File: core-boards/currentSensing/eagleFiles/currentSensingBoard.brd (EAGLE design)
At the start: 52 x 64.6 mm, 25 parts, among them J1 4-PIN_2MM-H, J2 3-PIN_2MM-H, J3 2-PIN_2MM-H, Q1 16MHz, X1 057-006-1

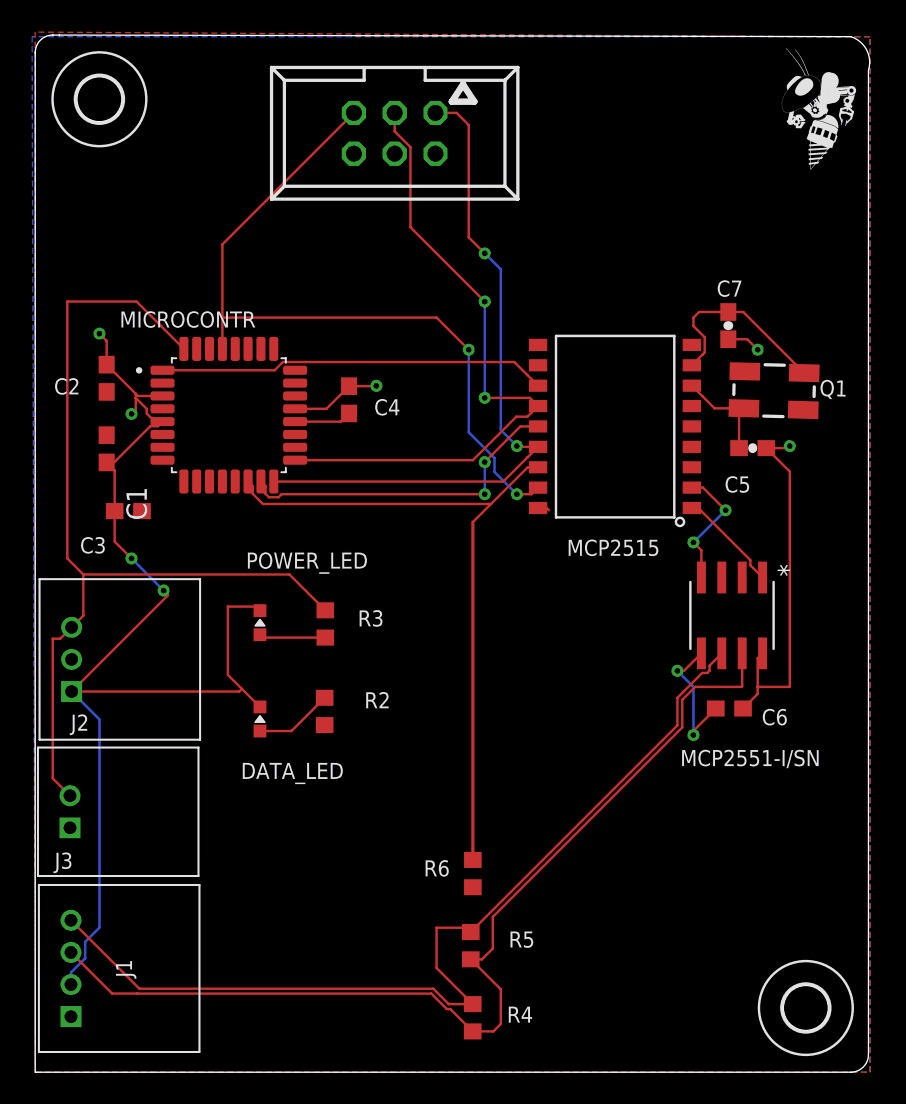
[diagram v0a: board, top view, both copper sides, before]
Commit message: Near-Finalized Current Sensing Board
I can't get the bottom edge to be round
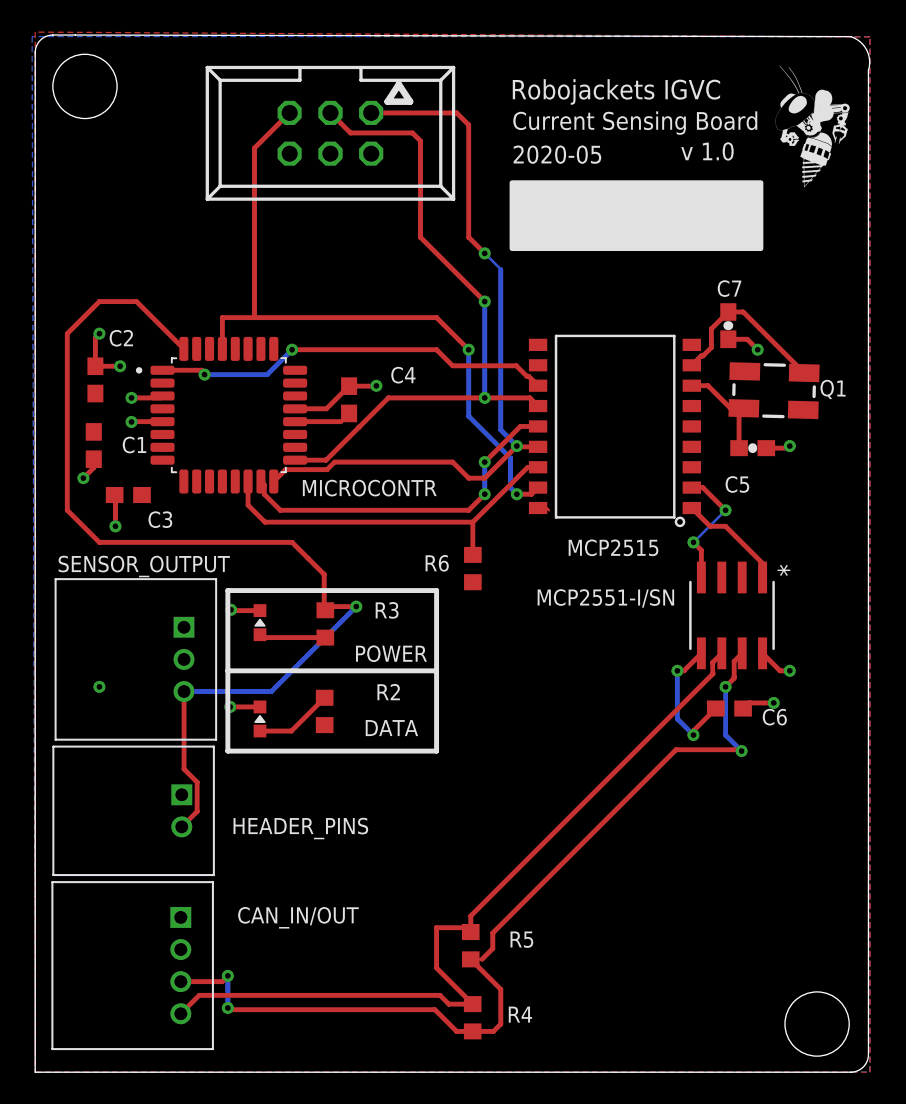
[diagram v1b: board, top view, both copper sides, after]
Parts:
- removed J1: 4-PIN_2MM-H, RoboJackets-Connectors:2MM-4-H
- removed J2: 3-PIN_2MM-H, RoboJackets-Connectors:2MM-3-H
- removed J3: 2-PIN_2MM-H, RoboJackets-Connectors:2MM-2-H
- removed U$2, U$3: (no value), holes:2,8
- removed X1: 057-006-1, con-panduit:057-006-1
- added CAN_IN/OUT: 4-PIN_2MM-H, RoboJackets-Connectors:2MM-4-H
- added HEADER_PINS: 2-PIN_2MM-H, RoboJackets-Connectors:2MM-2-H
- added ICSP: 057-006-1, con-panduit:057-006-1
- added SENSOR_OUTPUT: 3-PIN_2MM-H, RoboJackets-Connectors:2MM-3-H
- moved R6 19.0 mm to (27.3, 31.4)
- moved U$1 1.17 mm to (47.9, 55.1)
- moved C3 1.00 mm to (5.80, 36.0)
- moved C1 0.82 mm to (3.65, 39.0)
- moved C2 0.71 mm to (3.75, 43.1)
- renumbered DATA_LED to DATA, POWER_LED to POWER
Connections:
- net !RS: now also ICSP.5; no longer X1.5
- net +5V: now also CAN_IN/OUT.1, HEADER_PINS.1; no longer J1.1, J3.1
- net CAN_N: now also CAN_IN/OUT.4; no longer J1.4
- net CAN_P: now also CAN_IN/OUT.3; no longer J1.3
- net GND: now also CAN_IN/OUT.2, SENSOR_OUTPUT.1; no longer J1.2, J2.1
- net MISO: now also ICSP.1; no longer X1.1
- net SCK: now also ICSP.3; no longer X1.3
- net SENSOR_OUTPUT: now also HEADER_PINS.2, SENSOR_OUTPUT.3; no longer J2.3, J3.2
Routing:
- net GND: track 103.4 -> 28.6 mm, vias 7 -> 14
- net CAN_CS: track 42.5 -> 23.4 mm
- net CAN_N: track 59.1 -> 50.7 mm
- net SENSOR_OUTPUT: track 57.2 -> 64.1 mm, vias 0 -> 1
- net CAN_P: track 62.0 -> 57.5 mm, vias 0 -> 4
- net MISO: track 42.3 -> 45.8 mm
- net !RS: track 46.0 -> 43.5 mm
- net N$17: track 12.2 -> 10.8 mm
- net CAN_INT: track 24.2 -> 25.2 mm, vias 0 -> 2
- net SCK: track 40.1 -> 40.9 mm
- net MOSI: track 20.9 -> 21.7 mm
- net CAN_TX: track 6.23 -> 6.83 mm
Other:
- outline, holes or cut-outs redrawn
- board text added: "2020-05"
- board text added: "CAN_N"
- board text added: "CAN_P"
- board text added: "Current Sensing Board"
- board text added: "Robojackets IGVC"
- board text added: "v 1.0"

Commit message: Basic Updates Based on Notes
Needs help with a few things but I will discuss them in meeting.
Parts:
- moved DATA 6.94 mm to (20.1, 18.7)
- moved POWER 6.94 mm to (20.1, 24.7)
- moved R3 6.94 mm to (24.2, 24.6)
- moved R2 6.94 mm to (24.1, 19.2)
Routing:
- net SENSOR_OUTPUT: track 64.1 -> 75.9 mm, vias 1 -> 2

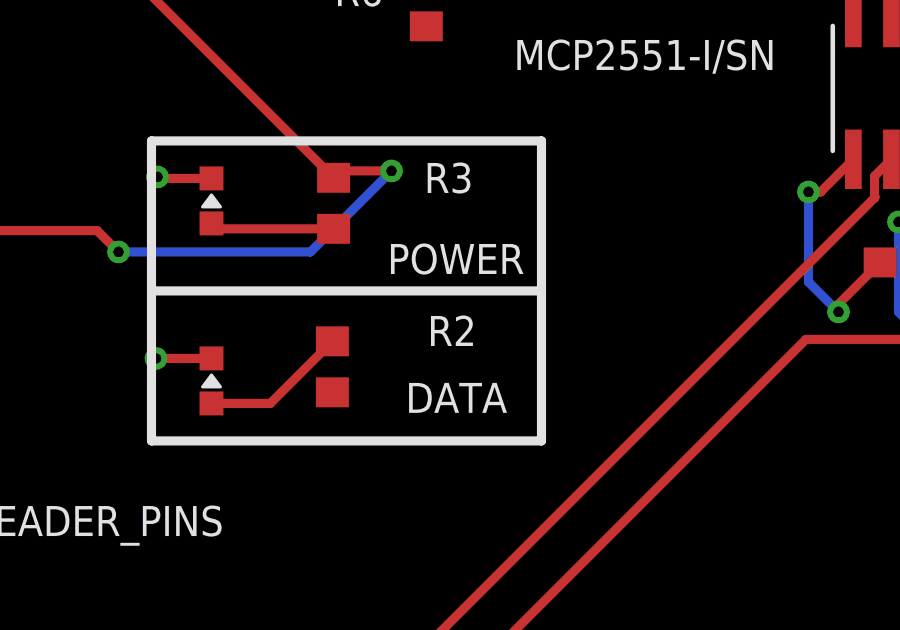
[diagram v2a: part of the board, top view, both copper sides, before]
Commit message: Leds fixed
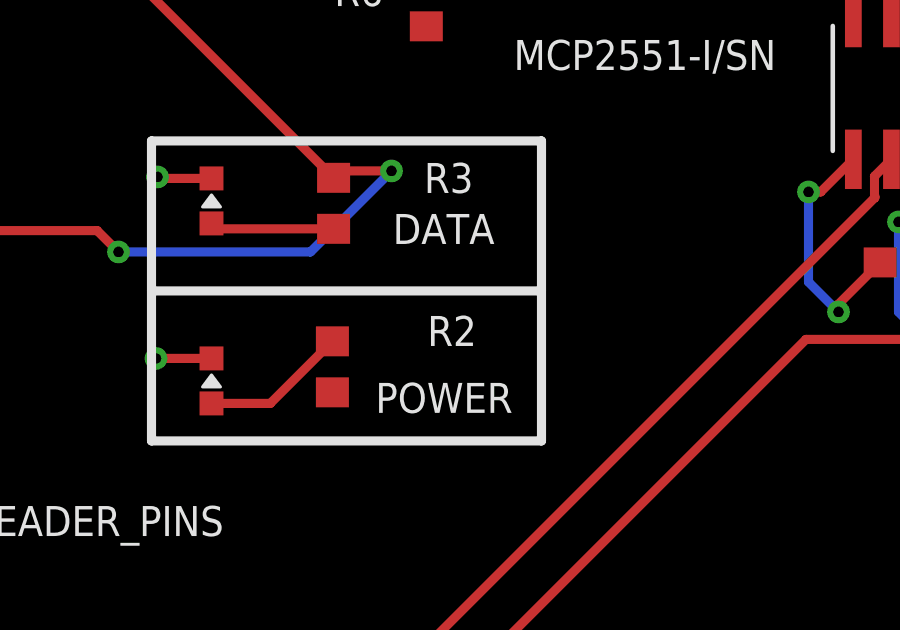
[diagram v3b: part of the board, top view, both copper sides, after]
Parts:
- DATA: value GREEN -> BLUE
- POWER: value BLUE -> GREEN
- moved DATA 6.00 mm to (20.1, 24.7)
- moved POWER 6.00 mm to (20.1, 18.7)
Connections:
- net N$2: now also DATA.A; no longer POWER.A
- net N$7: now also POWER.A; no longer DATA.A
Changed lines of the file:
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@@
 <attribute name="VALUE" x="24.2" y="53.93" size="1.778" layer="27" rot="R180"/>
 </element>
-<element name="DATA" library="RoboJackets-LEDs" package="CHIP-LED0603" value="GREEN" x="20.1" y="18.7" smashed="yes">
+<element name="POWER" library="RoboJackets-LEDs" package="CHIP-LED0603" value="GREEN" x="20.1" y="18.7" smashed="yes">
 <attribute name="DIGIKEY" value="160-1446-1-ND" x="20.1" y="18.7" size="1.778" layer="27" display="off"/>
 <attribute name="MPN" value="LTST-C191KGKT" x="20.1" y="18.7" size="1.778" layer="27" display="off"/>
-<attribute name="NAME" x="26.565" y="17.635" size="1" layer="25"/>
+<attribute name="NAME" x="25.565" y="17.635" size="1" layer="25"/>
 <attribute name="VALUE" x="22.005" y="18.065" size="1.27" layer="27" rot="R90"/>
 </element>
-<element name="POWER" library="RoboJackets-LEDs" package="CHIP-LED0603" value="BLUE" x="20.1" y="24.7" smashed="yes">
+<element name="DATA" library="RoboJackets-LEDs" package="CHIP-LED0603" value="BLUE" x="20.1" y="24.7" smashed="yes">
 <attribute name="DIGIKEY" value="160-1647-1-ND" x="20.1" y="24.7" size="1.778" layer="27" display="off"/>
 <attribute name="MPN" value="LTST-C191TBKT" x="20.1" y="24.7" size="1.778" layer="27" display="off"/>
-<attribute name="NAME" x="30.535" y="23.265" size="1" layer="25" rot="R180"/>
+<attribute name="NAME" x="29.535" y="24.265" size="1" layer="25" rot="R180"/>
 <attribute name="VALUE" x="22.005" y="24.065" size="1.27" layer="27" rot="R90"/>
 </element>
@@
 <wire x1="3.75" y1="45.75" x2="3.75" y2="43.97" width="0.3048" layer="1"/>
 <via x="4" y="46" extent="1-16" drill="0.35"/>
+<contactref element="POWER" pad="C"/>
 <contactref element="DATA" pad="C"/>
-<contactref element="POWER" pad="C"/>
 <wire x1="19.85" y1="25.7" x2="20.1" y2="25.45" width="0.1524" layer="1"/>
 <wire x1="45.54" y1="38.87" x2="46.87" y2="38.87" width="0.3048" layer="1"/>
@@
 <signal name="N$7">
 <contactref element="R2" pad="1"/>
-<contactref element="DATA" pad="A"/>
+<contactref element="POWER" pad="A"/>
 <wire x1="20.1" y1="17.95" x2="22.06" y2="17.95" width="0.3048" layer="1"/>
 <wire x1="22.06" y1="17.95" x2="24.13" y2="20.02" width="0.3048" layer="1"/>
@@
 </signal>
 <signal name="N$2">
-<contactref element="POWER" pad="A"/>
+<contactref element="DATA" pad="A"/>
 <contactref element="R3" pad="1"/>
 <wire x1="24.17" y1="23.77" x2="20.28" y2="23.77" width="0.3048" layer="1"/>

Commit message: Board Review Draft
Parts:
- added DEBUG: RED, RoboJackets-LEDs:CHIP-LED0603
- added R1: 1k, rcl:R0603
- moved R6 3.00 mm to (27.3, 28.4)
- renumbered DATA to OUTPUT, MICROCONTR to IC_MCU_8BIT
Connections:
- new net DEBUG: IC_MCU_8BIT.30, R1.2
- new net N$1: DEBUG.A, R1.1
- net GND: now also DEBUG.C
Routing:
- net DEBUG: track 0.00 -> 38.8 mm, vias 0 -> 2
- net SENSOR_OUTPUT: track 75.9 -> 58.5 mm, vias 2 -> 4
- net CAN_CS: track 23.4 -> 27.8 mm
- net N$1: track 0.00 -> 4.32 mm
- net CAN_INT: track 25.2 -> 27.5 mm
- net GND: track 28.6 -> 30.6 mm, vias 14 -> 15
- net CAN_N: track 50.7 -> 52.2 mm
- net !RS: track 43.5 -> 44.7 mm
- net CAN_P: track 57.5 -> 57.0 mm

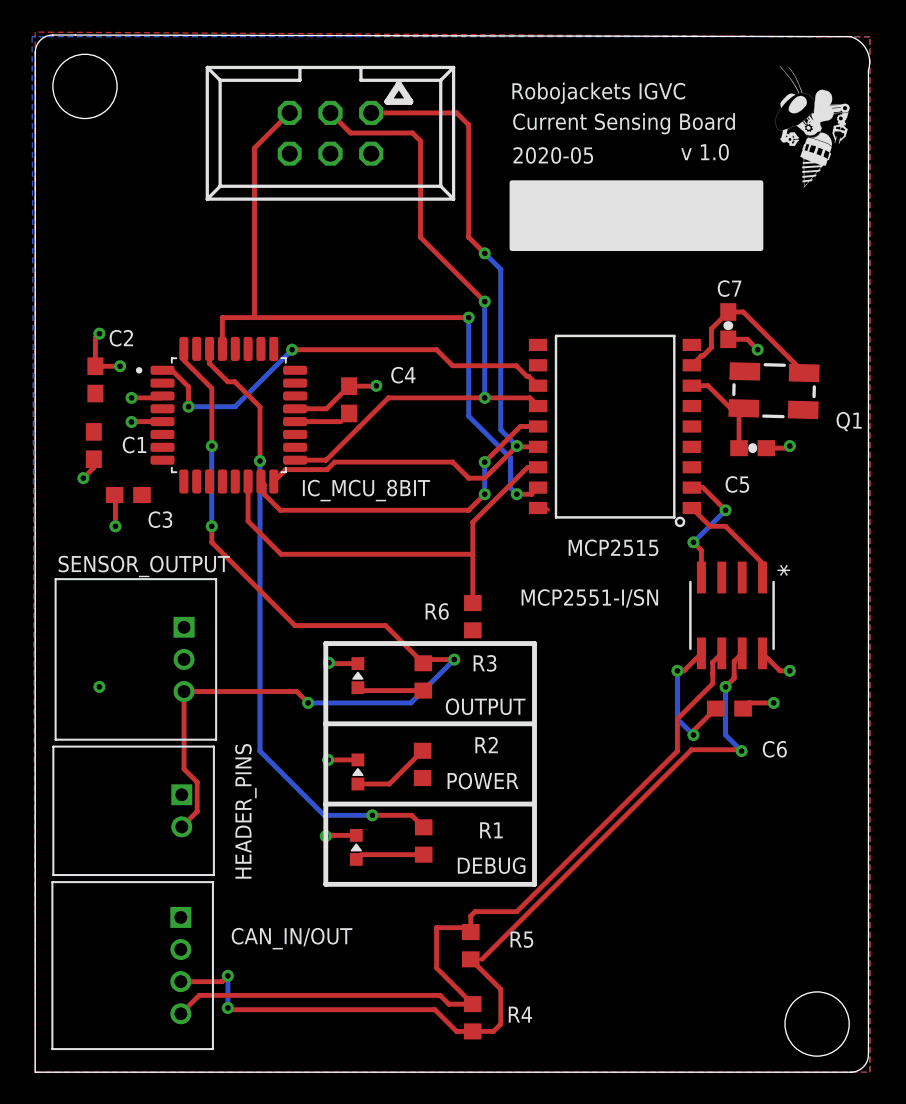
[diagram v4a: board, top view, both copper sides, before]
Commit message: Core Edit Current Sensing
Edited from core
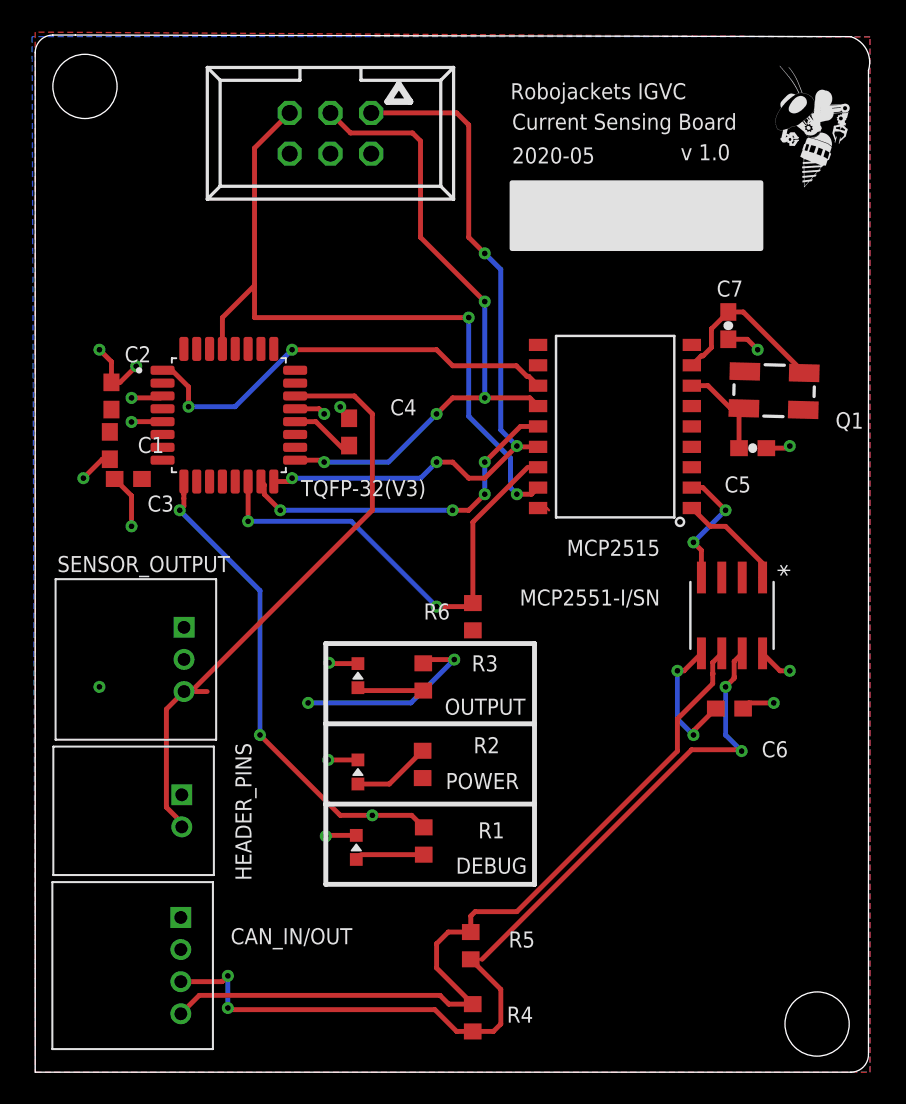
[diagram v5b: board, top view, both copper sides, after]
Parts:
- R1, R2, R3: value 1k -> 150
- moved C4 2.00 mm to (19.6, 39.9)
- moved C2 1.41 mm to (4.75, 42.1)
- moved C1 1.00 mm to (4.65, 39.0)
- moved C3 1.00 mm to (5.80, 37.0)
- renumbered IC_MCU_8BIT to TQFP-32(V3)
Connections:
- net DEBUG: now also TQFP-32(V3).9; no longer TQFP-32(V3).30
- net SENSOR_OUTPUT: now also TQFP-32(V3).22; no longer TQFP-32(V3).32
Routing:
- net DEBUG: track 38.8 -> 30.6 mm, vias 2 -> 3
- net SENSOR_OUTPUT: track 58.5 -> 50.7 mm, vias 4 -> 2
- net CAN_CS: track 27.8 -> 29.3 mm, vias 0 -> 2
- net !RS: track 44.7 -> 45.5 mm
- net N$6: track 3.57 -> 4.22 mm
- net SCK: track 40.9 -> 41.0 mm, vias 2 -> 4
- net GND: track 30.6 -> 30.5 mm, vias 15 -> 16
- net MISO: vias 2 -> 4
- net MOSI: vias 2 -> 4

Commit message: New Updates to Current Sensing
Nearing final stages
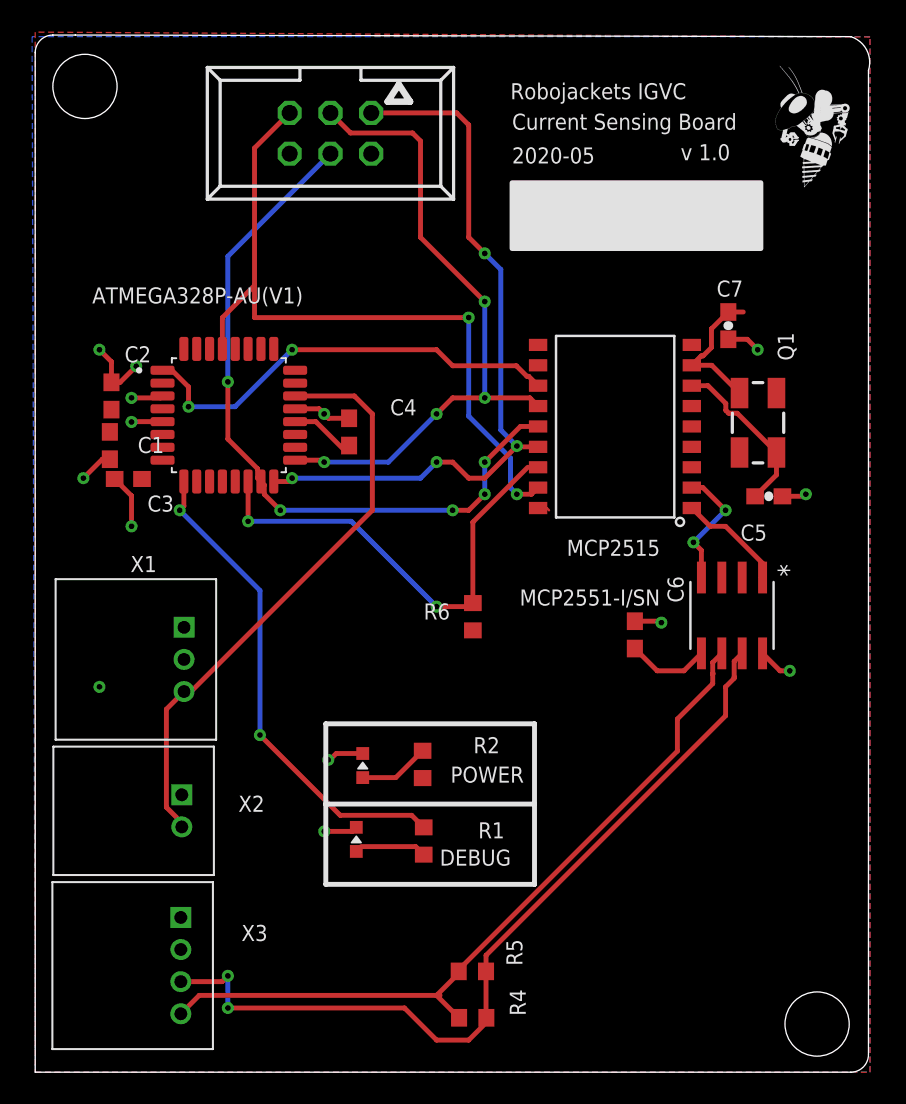
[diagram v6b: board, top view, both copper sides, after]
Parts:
- removed OUTPUT: BLUE, RoboJackets-LEDs:CHIP-LED0603
- removed R3: 150, rcl:R0603
- ATMEGA328P-AU(V1): value ATMEGA328P-AU -> ATMEGA328P-AU (V1)
- moved C6 7.47 mm to (37.4, 27.2), turned to 90 degrees
- moved C5 3.16 mm to (45.7, 35.9)
- moved Q1 2.24 mm to (45.0, 40.5), turned to 90 degrees
- moved R5 1.60 mm to (27.2, 6.28), turned to 0 degrees
- moved DEBUG 0.50 mm to (20.0, 14.5)
- moved POWER 0.50 mm to (20.4, 19.1)
- turned R4 to 0 degrees
- renumbered CAN_IN/OUT to X3, HEADER_PINS to X2, SENSOR_OUTPUT to X1, TQFP-32(V3) to ATMEGA328P-AU(V1)
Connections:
- removed net N$2: OUTPUT.A, R3.1
- net +5V: now also ICSP.2
- net GND: now also ICSP.6; no longer OUTPUT.C
- net MOSI: now also ICSP.4
- net SENSOR_OUTPUT: no longer R3.2
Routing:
- net MOSI: track 21.7 -> 45.6 mm, vias 4 -> 5
- net SENSOR_OUTPUT: track 50.7 -> 37.0 mm, vias 2 -> 0
- net CAN_P: track 57.0 -> 52.3 mm, vias 4 -> 2
- net CAN_N: track 51.8 -> 47.3 mm
- net N$2: track 4.14 -> 0.00 mm
- net N$18: track 6.43 -> 10.5 mm
- net N$4: track 8.59 -> 5.17 mm, vias 2 -> 0
- net N$17: track 10.8 -> 9.16 mm
- net GND: track 30.5 -> 29.2 mm, vias 16 -> 14
- net DEBUG: vias 3 -> 2
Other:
- board text added: "4mm"
